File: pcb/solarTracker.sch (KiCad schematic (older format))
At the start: 21 parts, among them U1 74HC4052, U2 STM32F071CBT6

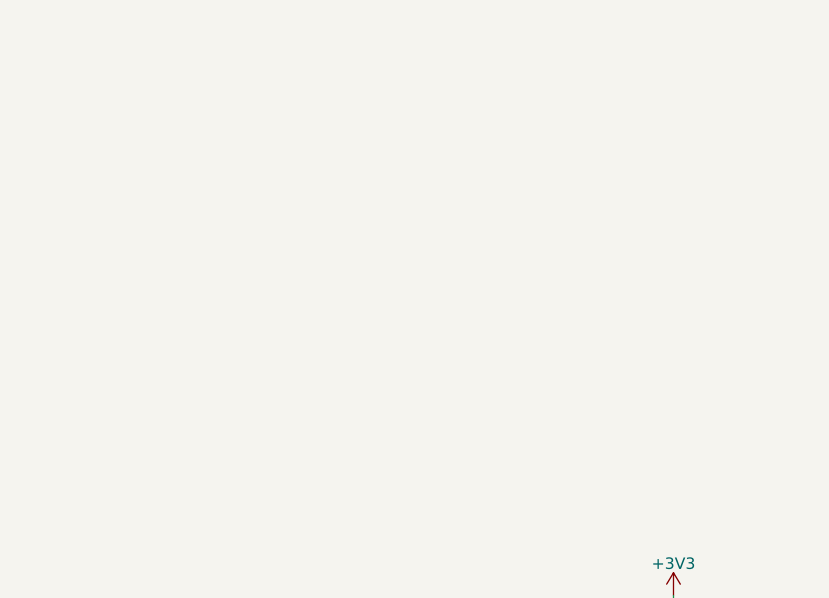
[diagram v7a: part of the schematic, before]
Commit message: add 3v3 converter
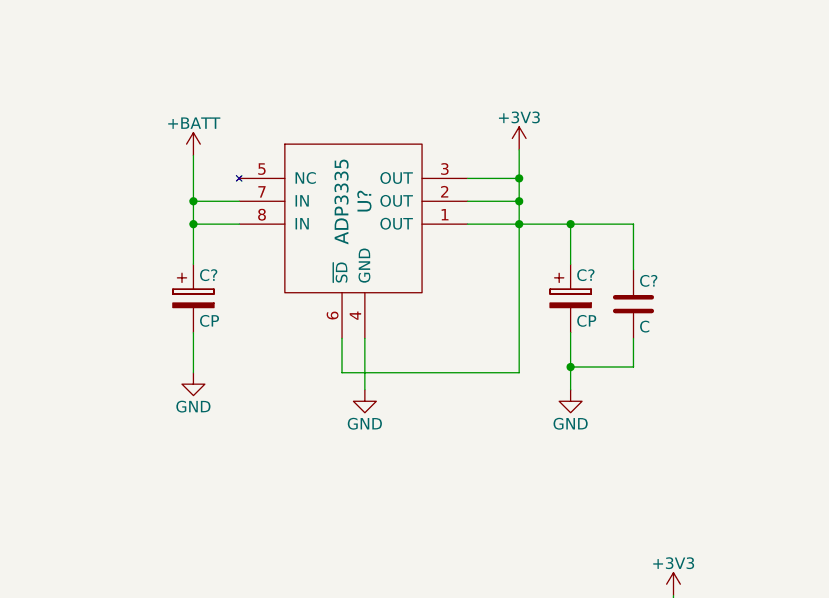
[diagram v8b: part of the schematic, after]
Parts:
- added C? (x2): CP, symbol CP
- added C?: C, symbol C
- added U?: ADP3335, symbol ADP3335
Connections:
- net +3V3: now also C?.1, C?.1, U?.1 (OUT), U?.2 (OUT), U?.3 (OUT), U?.6 (~SD)
- net +BATT: now also C?.1, U?.7 (IN), U?.8 (IN)
- net GND: now also C?.2, C?.2, C?.2, U?.4 (GND)
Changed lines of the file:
@@
 LIBS:servo
 LIBS:mc33063a
+LIBS:adp3335
 LIBS:solarTracker-cache
 EELAYER 25 0
@@
 Wire Wire Line
 	9225 5300 9300 5300
+$Comp
+L ADP3335 U?
+U 1 1 55C1468F
+P 4400 1550
+F 0 "U?" V 4500 1550 60  0000 C CNN
+F 1 "ADP3335" V 4400 1550 60  0000 C CNN
+F 2 "" H 4400 1700 60  0000 C CNN
+F 3 "" H 4400 1700 60  0000 C CNN
+	1    4400 1550
+	1    0    0    -1
+$EndComp
+Wire Wire Line
+	4500 2150 4500 2375
+$Comp
+L GND #PWR?
+U 1 1 55C149E2
+P 4500 2375
+F 0 "#PWR?" H 4500 2125 50  0001 C CNN
+F 1 "GND" H 4500 2225 50  0000 C CNN
+F 2 "" H 4500 2375 60  0000 C CNN
+F 3 "" H 4500 2375 60  0000 C CNN
+	1    4500 2375
+	1    0    0    -1
+$EndComp
+$Comp
+L +BATT #PWR?
+U 1 1 55C14A3A
+P 3750 1350
+F 0 "#PWR?" H 3750 1200 50  0001 C CNN
+F 1 "+BATT" H 3750 1490 50  0000 C CNN
+F 2 "" H 3750 1350 60  0000 C CNN
+F 3 "" H 3750 1350 60  0000 C CNN
+	1    3750 1350
+	1    0    0    -1
+$EndComp
+Wire Wire Line
+	3750 1350 3750 1825
+Wire Wire Line
+	3750 1550 3950 1550
+Wire Wire Line
+	3750 1650 3950 1650
+Connection ~ 3750 1550
+$Comp
+L +3V3 #PWR?
+U 1 1 55C14BCB
+P 5175 1325
+F 0 "#PWR?" H 5175 1175 50  0001 C CNN
+F 1 "+3V3" H 5175 1465 50  0000 C CNN
+F 2 "" H 5175 1325 60  0000 C CNN
+F 3 "" H 5175 1325 60  0000 C CNN
+	1    5175 1325
+	1    0    0    -1
+$EndComp
+Wire Wire Line
+	5175 1325 5175 2300
+Wire Wire Line
+	5175 1450 4950 1450
+Wire Wire Line
+	5175 1550 4950 1550
+Connection ~ 5175 1450
+Wire Wire Line
+	4950 1650 5675 1650
+Connection ~ 5175 1550
+Wire Wire Line
+	4400 2150 4400 2300
+Wire Wire Line
+	4400 2300 5175 2300
+Connection ~ 5175 1650
+$Comp
+L CP C?
+U 1 1 55C150CE
+P 3750 1975
+F 0 "C?" H 3775 2075 50  0000 L CNN
+F 1 "CP" H 3775 1875 50  0000 L CNN
+F 2 "" H 3788 1825 30  0000 C CNN
+F 3 "" H 3750 1975 60  0000 C CNN
+	1    3750 1975
+	1    0    0    -1
+$EndComp
+$Comp
+L CP C?
+U 1 1 55C1516A
+P 5400 1975
+F 0 "C?" H 5425 2075 50  0000 L CNN
+F 1 "CP" H 5425 1875 50  0000 L CNN
+F 2 "" H 5438 1825 30  0000 C CNN
+F 3 "" H 5400 1975 60  0000 C CNN
+	1    5400 1975
+	1    0    0    -1
+$EndComp
+Wire Wire Line
+	5400 1650 5400 1825
+Wire Wire Line
+	5400 2125 5400 2375
+$Comp
+L GND #PWR?
+U 1 1 55C153FB
+P 5400 2375
+F 0 "#PWR?" H 5400 2125 50  0001 C CNN
+F 1 "GND" H 5400 2225 50  0000 C CNN
+F 2 "" H 5400 2375 60  0000 C CNN
+F 3 "" H 5400 2375 60  0000 C CNN
+	1    5400 2375
+	1    0    0    -1
+$EndComp
+Wire Wire Line
+	5675 1650 5675 1850
+Connection ~ 5400 1650
+$Comp
+L C C?
+U 1 1 55C15504
+P 5675 2000
+F 0 "C?" H 5700 2100 50  0000 L CNN
+F 1 "C" H 5700 1900 50  0000 L CNN
+F 2 "" H 5713 1850 30  0000 C CNN
+F 3 "" H 5675 2000 60  0000 C CNN
+	1    5675 2000
+	1    0    0    -1
+$EndComp
+Wire Wire Line
+	5675 2150 5675 2275
+Wire Wire Line
+	5675 2275 5400 2275
+Connection ~ 5400 2275
+Connection ~ 3750 1650
+Wire Wire Line
+	3750 2125 3750 2300
+$Comp
+L GND #PWR?
+U 1 1 55C159D0
+P 3750 2300
+F 0 "#PWR?" H 3750 2050 50  0001 C CNN
+F 1 "GND" H 3750 2150 50  0000 C CNN
+F 2 "" H 3750 2300 60  0000 C CNN
+F 3 "" H 3750 2300 60  0000 C CNN
+	1    3750 2300
+	1    0    0    -1
+$EndComp
 $EndSCHEMATC
